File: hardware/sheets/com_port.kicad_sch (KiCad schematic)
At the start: 28 parts, among them J1 DE9_Pins, J2 Conn_01x03, J3 Conn_01x04, U1 TL16C550C, U2 MAX3241, U3 74HC04, U4 74HC08, U5 74HC08, U6 74LVC125A, Y1 1.8432MHz

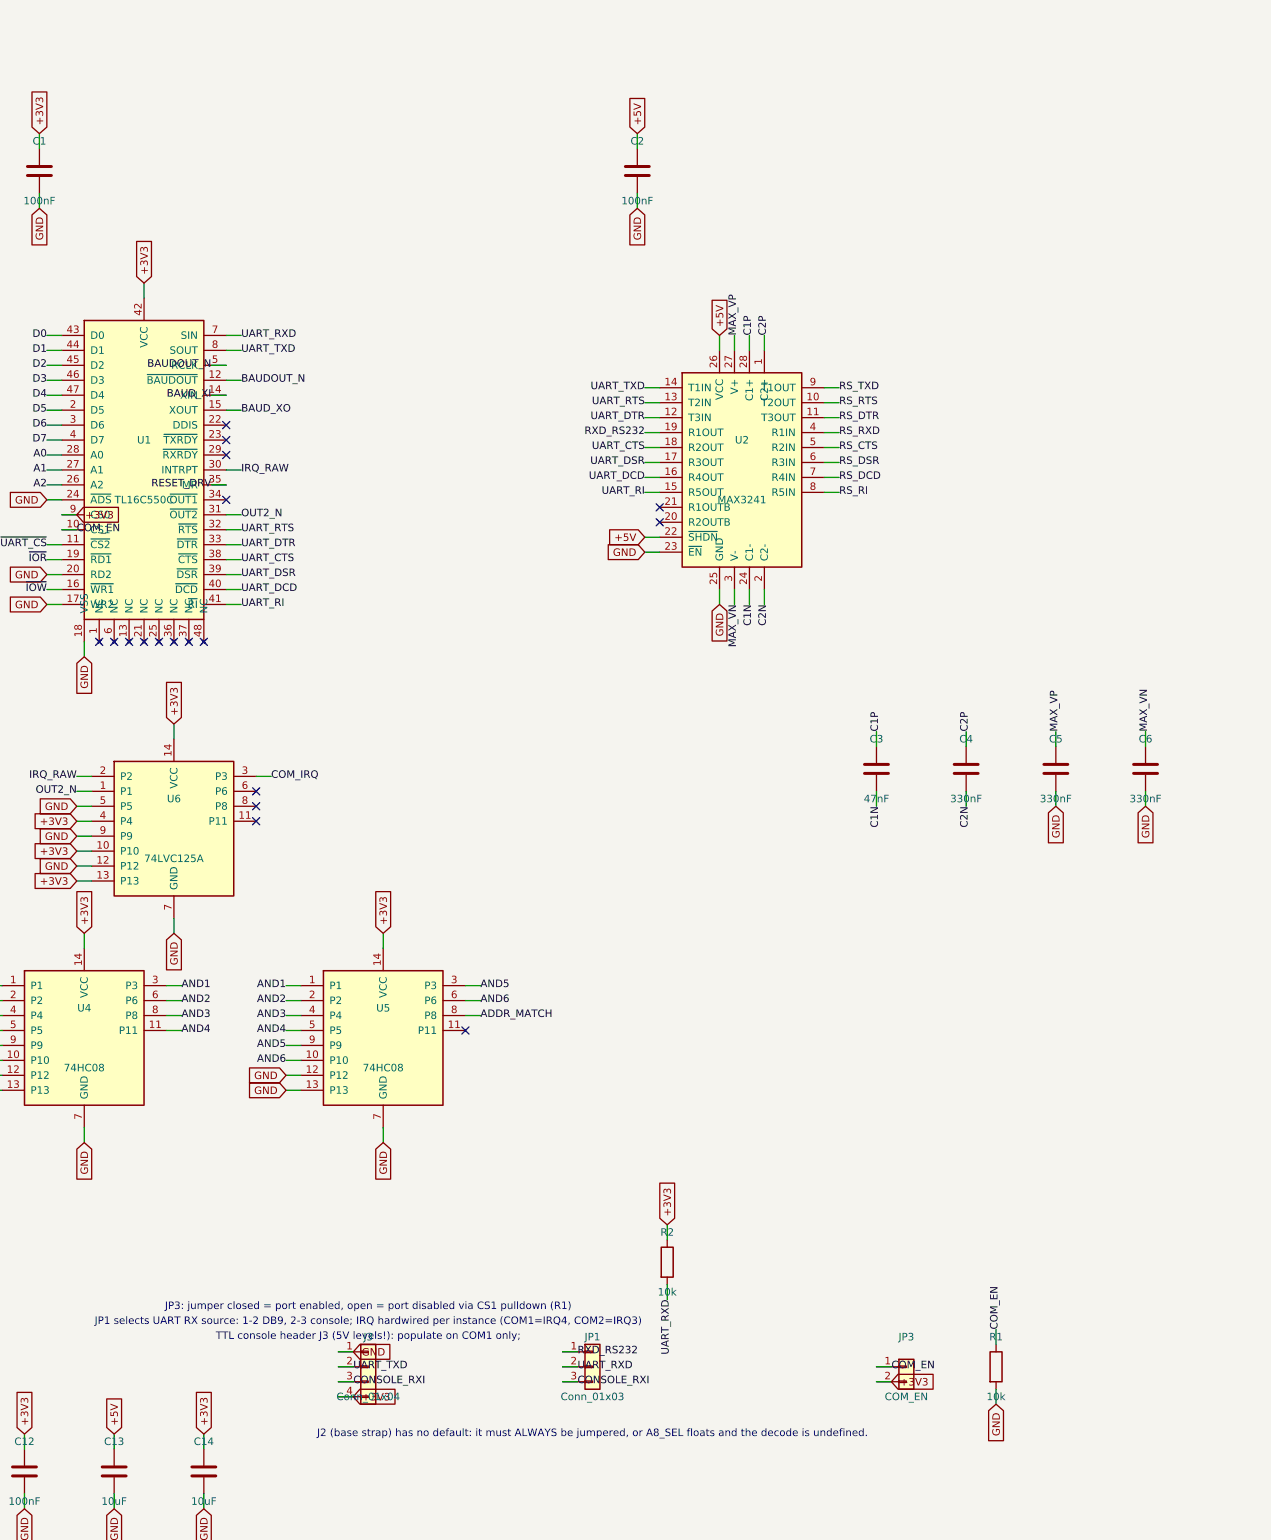
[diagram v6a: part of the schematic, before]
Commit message: 3.3V redesign: final-review fix wave (6 findings)
Reviewer-verified fixes, all at the generator level + regenerated outputs:

1. (Critical) bus_mcu U17 '04 @+3V3 had the V20's 5V HLDA on its input ->
   value-override to 74LVC04A (5V-tolerant input; parts.py binds C282341).
2. network R7 (AEN_CHIP park) +5V -> +3V3: it also feeds U5's '138 @+3V3;
   RTL8019AS AEN is 5V-TTL so 3.3V still reads high.
3. sidecar buf244(): tie unused '244 A inputs to GND, no_connect the Y
   outputs (U1105: 6 spare, U1108: 7) -- no floating always-enabled inputs.
4. MAX3241s (both com_port instances) +5V -> +3V3; charge-pump caps to the
   datasheet 3.0-3.6V column (all 0.1uF). Removes the 5V-R*OUT-into-3.3V-UART
   receiver path; com_port now has no +5V rail.
5. V20 READY/HOLD re-buffered through cpu_core U13's 3 spare '04 gates (zero
   package cost). READY = 2 gates (non-inverting), single-driver (no fold).
   HOLD = 1 inverting gate -> FIRMWARE MUST DRIVE HOLD ACTIVE-LOW at GPIO25
   (mxbus HOLD name intact). U13 nudged to clear a stub collision with U12.
6. Docs census + staleness: rewrote the 5V census to post-fix reality across
   CLAUDE.md, spec, design doc, README, irq-io-map (IRQ8 soft-PIC/undriven),
   parts.py header notes.

Build exit 0; check_parts 0 problems; all five sheets validate with zero
structural violations. Netlist evidence in questions-*.md.

Co-Authored-By: Claude Fable 5 <noreply@anthropic.com>
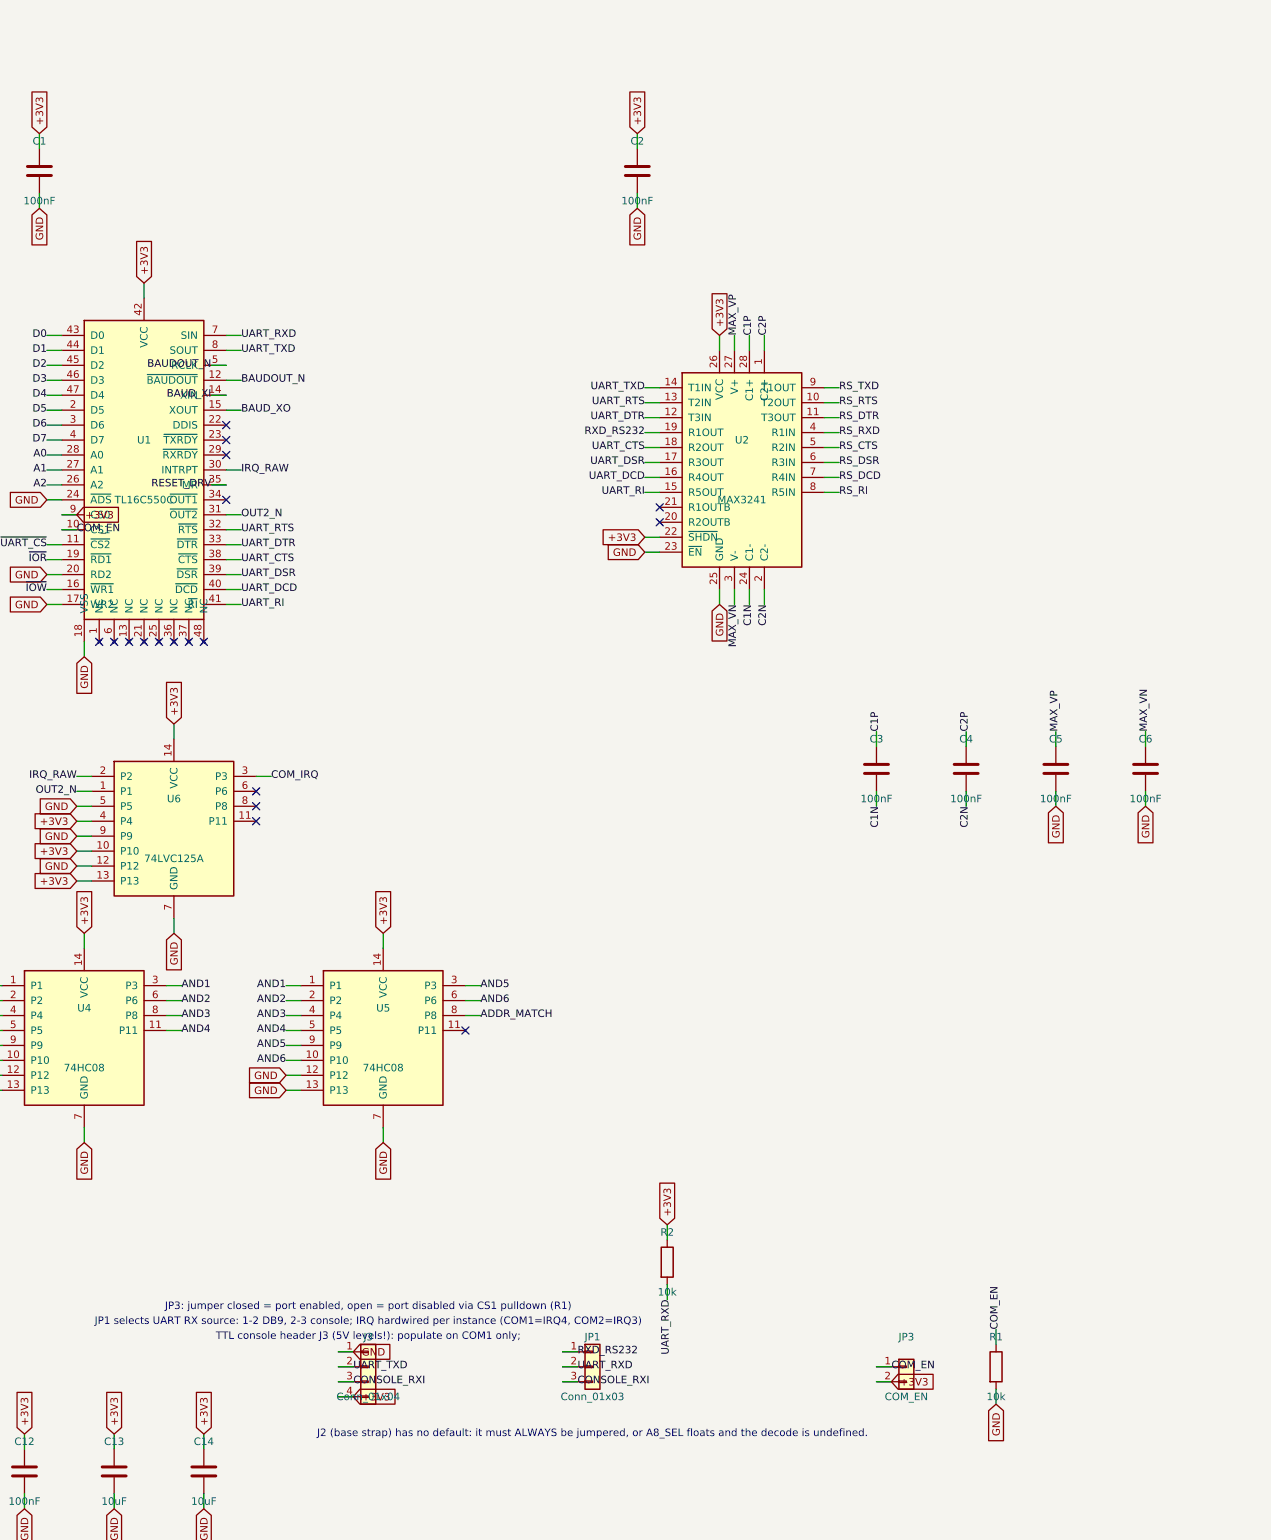
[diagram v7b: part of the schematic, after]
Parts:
- C3: value 47nF -> 100nF; LCSC Part Num C1622 -> C14663
- C4, C5, C6: value 330nF -> 100nF; LCSC Part Num C1615 -> C14663
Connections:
- net +5V is gone; now on net +3V3: C13.1, C2.1, U2.22 (~{SHDN}), U2.26 (VCC)
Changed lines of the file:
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@@
 		)
 	)
-	(global_label "+5V"
+	(global_label "+3V3"
 		(shape input)
 		(at 224.79 78.74 90)
@@
 		)
 	)
-	(global_label "+5V"
+	(global_label "+3V3"
 		(shape input)
 		(at 212.09 113.03 180)
@@
 		)
 	)
-	(global_label "+5V"
+	(global_label "+3V3"
 		(shape input)
 		(at 210.82 44.45 90)
@@
 		)
 	)
-	(global_label "+5V"
+	(global_label "+3V3"
 		(shape input)
 		(at 121.92 265.43 90)
@@
 			)
 		)
-		(property "Value" "47nF"
+		(property "Value" "100nF"
 			(at 251.46 157.48 0)
 			(effects
@@
 			)
 		)
-		(property "LCSC Part Num" "C1622"
+		(property "LCSC Part Num" "C14663"
 			(at 251.46 152.4 0)
 			(effects
@@
 			)
 		)
-		(property "Value" "330nF"
+		(property "Value" "100nF"
 			(at 266.7 157.48 0)
 			(effects
@@
 			)
 		)
-		(property "LCSC Part Num" "C1615"
+		(property "LCSC Part Num" "C14663"
 			(at 266.7 152.4 0)
 			(effects
@@
 			)
 		)
-		(property "Value" "330nF"
+		(property "Value" "100nF"
 			(at 281.94 157.48 0)
 			(effects
@@
 			)
 		)
-		(property "LCSC Part Num" "C1615"
+		(property "LCSC Part Num" "C14663"
 			(at 281.94 152.4 0)
 			(effects
@@
 			)
 		)
-		(property "Value" "330nF"
+		(property "Value" "100nF"
 			(at 297.18 157.48 0)
 			(effects
@@
 			)
 		)
-		(property "LCSC Part Num" "C1615"
+		(property "LCSC Part Num" "C14663"
 			(at 297.18 152.4 0)
 			(effects

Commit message: com_port: merge COM1+COM2 onto one sheet with shared decode/IRQ glue
One address decoder serves both ports (0x3F8/0x2F8 differ only in A8:
common A3-A7,A9,~AEN term ANDed with A8/~A8) and one 74LVC125A gates
both IRQs -- glue drops from 8 chips to 4, COM subsystem 12 ICs -> 8
(56 comps -> 41). Base addresses hardwired (J2 straps existed only
because one generic sheet was instanced at both addresses); console
header + RX select drawn once on COM1; enables now JP3/JP4; interface
exposes IRQ4/IRQ3 directly instead of the COM_IRQ remap. Sheet moves
to A2 paper; validate_sheet.py now honors PAPER. Docs/notes aligned.

Co-Authored-By: Claude Fable 5 <noreply@anthropic.com>
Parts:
- removed J2: Conn_01x03, Connector_PinHeader_2.54mm:PinHeader_1x03_P2.54mm_Vertical, symbol Connector_Generic:Conn_01x03
- removed U3: 74HC04, Package_SO:SOIC-14_3.9x8.7mm_P1.27mm, symbol mini-xt:74HCT04
- removed U4, U5: 74HC08, Package_SO:SOIC-14_3.9x8.7mm_P1.27mm, symbol mini-xt:74HCT08
- removed U6: 74LVC125A, Package_SO:SOIC-14_3.9x8.7mm_P1.27mm, symbol mini-xt:74HCT125
- added C15, C16: 22pF, Capacitor_SMD:C_0603_1608Metric, symbol Device:C
- added C17, C18, C19, C20: 100nF, Capacitor_SMD:C_0603_1608Metric, symbol Device:C
- added C21, C22: 10uF, Capacitor_SMD:C_0805_2012Metric, symbol Device:C
- added J2: DE9_Pins, Connector_Dsub:DSUB-9_Pins_Horizontal_P2.77x2.84mm_EdgePinOffset9.90mm_Housed_MountingHolesOffset11.32mm, symbol Connector:DE9_Pins
- added JP4: COM2_EN, Connector_PinHeader_2.54mm:PinHeader_1x02_P2.54mm_Vertical, symbol Connector_Generic:Conn_01x02
- added R3: 10k, Resistor_SMD:R_0603_1608Metric, symbol Device:R
- added U3: TL16C550C, Package_QFP:LQFP-48_7x7mm_P0.5mm, symbol mini-xt:TL16C550PT
- added U4: MAX3241, Package_SO:SSOP-28_5.3x10.2mm_P0.65mm, symbol mini-xt:MAX3241
- added U5: 74HC04, Package_SO:SOIC-14_3.9x8.7mm_P1.27mm, symbol mini-xt:74HCT04
- added U6, U7: 74HC08, Package_SO:SOIC-14_3.9x8.7mm_P1.27mm, symbol mini-xt:74HCT08
- added U8: 74LVC125A, Package_SO:SOIC-14_3.9x8.7mm_P1.27mm, symbol mini-xt:74HCT125
- added Y2: 1.8432MHz, Crystal:Crystal_HC49-U_Vertical, symbol Device:Crystal
- C13, C14: value 10uF -> 100nF; footprint Capacitor_SMD:C_0805_2012Metric -> Capacitor_SMD:C_0603_1608Metric; LCSC Part Num C15850 -> C14663
- JP3: value COM_EN -> COM1_EN
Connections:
- net +3V3: now also C1.2, C10.2, C13.2, C14.2, C2.2, C5.2, C6.2, C7.2, C8.2, C9.2, J1.5, J3.1 (Pin_1), R1.2, R2.2, U1.17 (WR2), U1.18 (VSS), U1.20 (RD2), U1.24 (~{ADS}), U2.23 (~{EN}), U2.25 (GND), C15.2, C16.2, C17.1, C17.2, C18.1, C18.2, C19.1, C19.2, C20.1, C20.2, C21.1, C21.2, C22.1, C22.2, J2.5, JP4.2 (Pin_2), R3.1, U3.17 (WR2), U3.18 (VSS), U3.20 (RD2), U3.24 (~{ADS}), U3.42 (VCC), U3.9 (CS0), U4.22 (~{SHDN}), U4.23 (~{EN}), U4.25 (GND), U4.26 (VCC), U5.11 (P11), U5.13 (P13), U5.14 (VCC), U5.7 (GND), U6.14 (VCC), U6.7 (GND), U7.14 (VCC), U7.7 (GND), U8.10 (P10), U8.12 (P12), U8.13 (P13), U8.14 (VCC), U8.7 (GND), U8.9 (P9); no longer C11.1, C12.1, C13.1, C14.1, R2.1
- net A0: now also U3.28 (A0)
- net A1: now also U3.27 (A1)
- net A2: now also U3.26 (A2)
- net A3: now also U6.1 (P1)
- net A4: now also U6.2 (P2)
- net A5: now also U6.4 (P4)
- net A6: now also U6.5 (P5)
- net A7: now also U6.9 (P9)
- net A8: now also U5.1 (P1), U7.10 (P10)
- net A8_N: now also U5.2 (P2), U7.13 (P13)
- net A9: now also U6.10 (P10)
- net AEN: now also U5.3 (P3)
- net AEN_N: now also U5.4 (P4), U7.2 (P2)
- net AND1: now also U6.12 (P12), U6.3 (P3)
- net AND2: now also U6.13 (P13), U6.6 (P6)
- net AND3: now also U6.8 (P8), U7.1 (P1)
- net AND4: now also U6.11 (P11), U7.4 (P4)
- net AND5: now also U7.3 (P3), U7.5 (P5)
- net D0: now also U3.43 (D0)
- net D1: now also U3.44 (D1)
- net D2: now also U3.45 (D2)
- net D3: now also U3.46 (D3)
- net D4: now also U3.47 (D4)
- net D5: now also U3.2 (D5)
- net D6: now also U3.3 (D6)
- net D7: now also U3.4 (D7)
- net RESET_DRV: now also U3.35 (MR)
- net ~{IOR}: now also U3.19 (~{RD1})
- net ~{IOW}: now also U3.16 (~{WR1})
- net BAUDOUT_N renamed BAUDOUT1_N
- net BAUD_XI renamed BAUD_XI1
- net BAUD_XO renamed BAUD_XO1
- net C1N renamed C1N1
- net C1P renamed C1P1
- net C2N renamed C2N1
- net C2P renamed C2P1
- net COM_EN renamed COM_EN1
- removed net GND: C1.2, C10.2, C11.2, C12.2, C13.2, C14.2, C2.2, C5.2, C6.2, C7.2, C8.2, C9.2, J1.5, J3.1 (Pin_1), R1.2, U1.17 (WR2), U1.18 (VSS), U1.20 (RD2), U1.24 (~{ADS}), U2.23 (~{EN}), U2.25 (GND)
- net IRQ_RAW renamed IRQ_RAW1
- net IRQ_RAW1: now also U8.2 (P2)
- net MAX_VN renamed MAX_VN1
- net MAX_VP renamed MAX_VP1
- net OUT2_N renamed OUT2_N1
- net OUT2_N1: now also U8.1 (P1)
- net RS_CTS renamed RS_CTS1
- net RS_DCD renamed RS_DCD1
- net RS_DSR renamed RS_DSR1
- net RS_DTR renamed RS_DTR1
- net RS_RI renamed RS_RI1
- net RS_RTS renamed RS_RTS1
- net RS_RXD renamed RS_RXD1
- net RS_TXD renamed RS_TXD1
- net UART_CTS renamed UART_CTS1
- net UART_DCD renamed UART_DCD1
- net UART_DSR renamed UART_DSR1
- net UART_DTR renamed UART_DTR1
- net UART_RI renamed UART_RI1
- net UART_RTS renamed UART_RTS1
- net UART_RXD renamed UART_RXD1
- net UART_RXD1: now also R3.2; no longer R2.2
- net UART_TXD renamed UART_TXD1
- net ~{UART_CS} renamed ~{UART_CS1}
- net ~{UART_CS1}: now also U5.6 (P6)
- new net ADDR_MATCH1: U5.5 (P5), U7.8 (P8)
- new net ADDR_MATCH2: U5.9 (P9), U7.11 (P11)
- new net BAUDOUT2_N: U3.12 (~{BAUDOUT}), U3.5 (RCLK)
- new net BAUD_XI2: C15.1, U3.14 (XIN), Y2.1
- new net BAUD_XO2: C16.1, U3.15 (XOUT), Y2.2
- new net C1N2: C11.2, U4.24 (C1-)
- new net C1P2: C11.1, U4.28 (C1+)
- new net C2N2: C12.2, U4.2 (C2-)
- new net C2P2: C12.1, U4.1 (C2+)
- new net COM_DEC: U7.12 (P12), U7.6 (P6), U7.9 (P9)
- new net COM_EN2: JP4.1 (Pin_1), R2.1, U3.10 (CS1)
- new net IRQ3: U8.6 (P6)
- new net IRQ4: U8.3 (P3)
- new net IRQ_RAW2: U3.30 (INTRPT), U8.5 (P5)
- new net MAX_VN2: C14.1, U4.3 (V-)
- new net MAX_VP2: C13.1, U4.27 (V+)
- new net OUT2_N2: U3.31 (~{OUT2}), U8.4 (P4)
- new net RS_CTS2: J2.8, U4.5 (R2IN)
- new net RS_DCD2: J2.1, U4.7 (R4IN)
- new net RS_DSR2: J2.6, U4.6 (R3IN)
- new net RS_DTR2: J2.4, U4.11 (T3OUT)
- new net RS_RI2: J2.9, U4.8 (R5IN)
- new net RS_RTS2: J2.7, U4.10 (T2OUT)
- new net RS_RXD2: J2.2, U4.4 (R1IN)
- new net RS_TXD2: J2.3, U4.9 (T1OUT)
- new net UART_CTS2: U3.38 (~{CTS}), U4.18 (R2OUT)
- new net UART_DCD2: U3.40 (~{DCD}), U4.16 (R4OUT)
- new net UART_DSR2: U3.39 (~{DSR}), U4.17 (R3OUT)
- new net UART_DTR2: U3.33 (~{DTR}), U4.12 (T3IN)
- new net UART_RI2: U3.41 (~{RI}), U4.15 (R5OUT)
- new net UART_RTS2: U3.32 (~{RTS}), U4.13 (T2IN)
- new net UART_RXD2: U3.7 (SIN), U4.19 (R1OUT)
- new net UART_TXD2: U3.8 (SOUT), U4.14 (T1IN)
- new net ~{UART_CS2}: U3.11 (~{CS2}), U5.8 (P8)
- no-connect marks 21 -> 32
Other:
- note added: "Base addresses hardwired: COM1 0x3F8 (A8 AND), COM2 0x2F8 (~A8 AND); IRQs hardwired COM1=IRQ4, COM2=IRQ3"
- note added: "JP1 selects COM1 UART RX source: 1-2 DB9, 2-3 TTL console (J3, 3.3V levels)"
- note added: "JP3/JP4: jumper closed = port enabled, open = port disabled via CS1 pulldown"
- note removed: "Base-address strap J2: jumper A8 (0x3F8/COM1) or ~A8 (0x2F8/COM2)"
- note removed: "J2 (base strap) has no default: it must ALWAYS be jumpered, or A8_SEL floats and the decode is undefined."
- note removed: "JP1 selects UART RX source: 1-2 DB9, 2-3 console; IRQ hardwired per instance (COM1=IRQ4, COM2=IRQ3)"
- note removed: "JP3: jumper closed = port enabled, open = port disabled via CS1 pulldown (R1)"
- note removed: "TTL console header J3 (5V levels!): populate on COM1 only;"
- title: COM port -- 16C550 UART + MAX3241 + DB9 (instanced x2) -> COM1+COM2 -- 2x 16C550 UART + MAX3241 + DB9, shared decode
